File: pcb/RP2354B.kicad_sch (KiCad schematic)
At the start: 29 parts, among them J1 Conn_01x03_MountingPin, SW1 SW_Push, SW2 SW_Push, U2 RP2354B, Y1 ABM8-272-T3

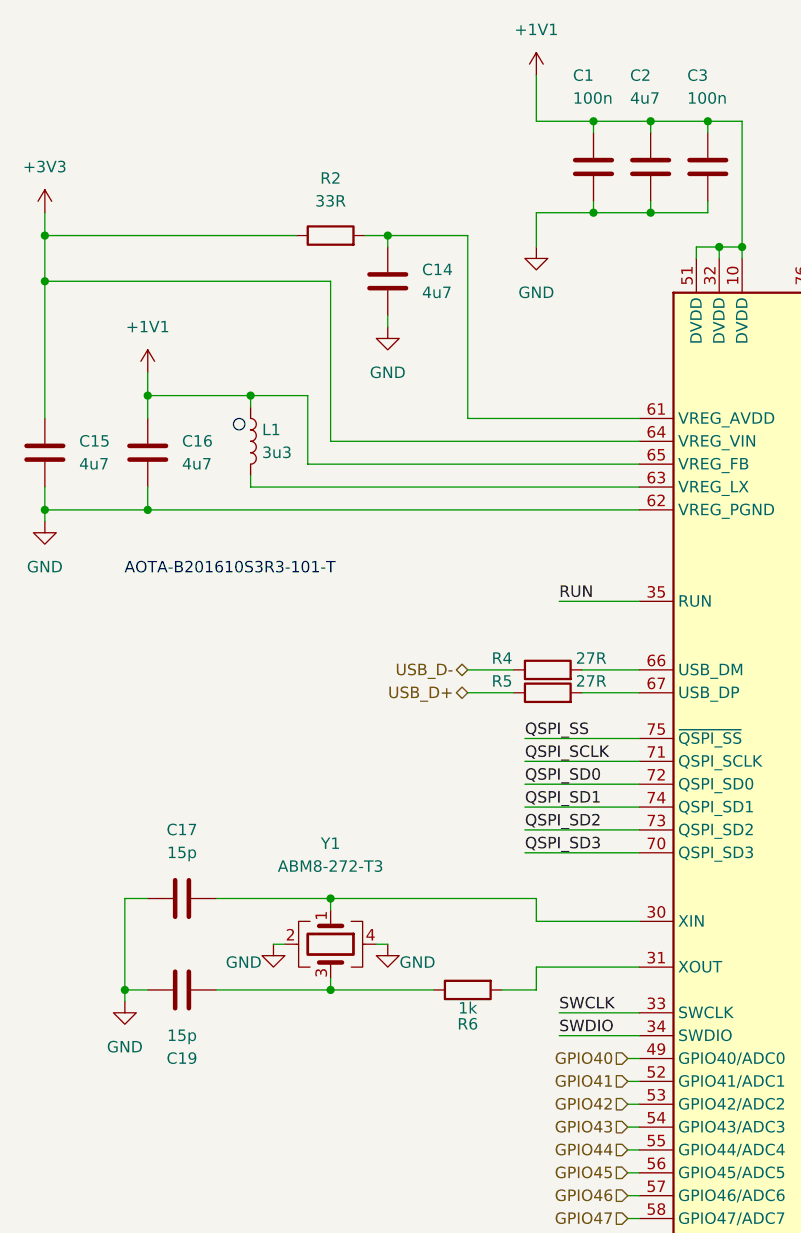
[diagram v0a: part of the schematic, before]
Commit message: Fixed 1V1 trace and added a bit to ADC schematic
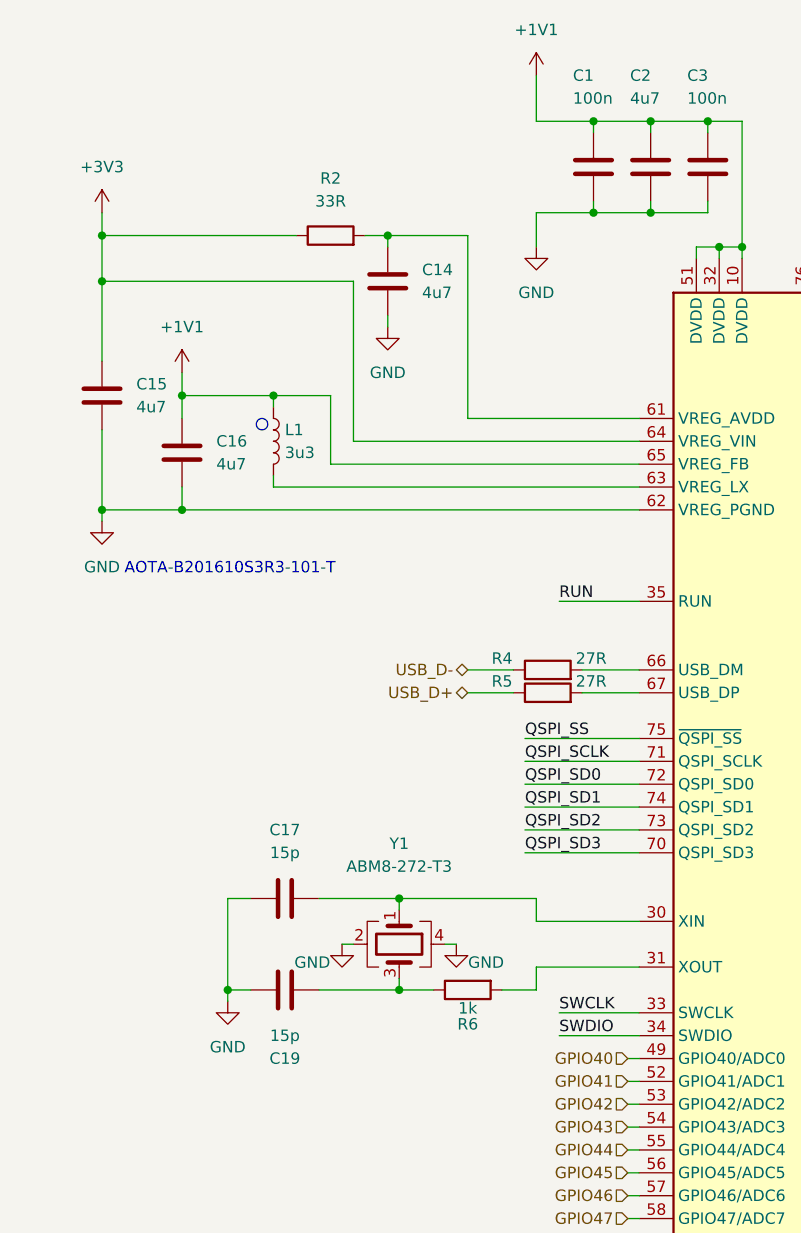
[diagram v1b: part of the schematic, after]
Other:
- moved on the sheet: C15, C16, C17, C19, L1, Y1

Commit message: moved stuff around, started on display
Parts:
- C15, C16: footprint RP2350_80QFN_minimal:C_0402_1005Metric_small_pads -> RP2354B_MINIMAL:C_0402_1005Metric_small_pads
- L1: footprint RP2350_80QFN_minimal:L_pol_2016 -> RP2354B_MINIMAL:L_pol_2016
- U2: footprint RP2350_80QFN_minimal:RP2350-QFN-80-1EP_10x10_P0.4mm_EP3.4x3.4mm_ThermalVias -> RP2354B_MINIMAL:RP2350-QFN-80-1EP_10x10_P0.4mm_EP3.4x3.4mm_ThermalVias
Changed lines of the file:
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@@
 			)
 		)
-		(property "Footprint" "RP2350_80QFN_minimal:C_0402_1005Metric_small_pads"
+		(property "Footprint" "RP2354B_MINIMAL:C_0402_1005Metric_small_pads"
 			(at 32.7152 63.5 0)
 			(hide yes)
@@
 			)
 		)
-		(property "Footprint" "RP2350_80QFN_minimal:L_pol_2016"
+		(property "Footprint" "RP2354B_MINIMAL:L_pol_2016"
 			(at 50.8 64.77 0)
 			(hide yes)
@@
 			)
 		)
-		(property "Footprint" "RP2350_80QFN_minimal:C_0402_1005Metric_small_pads"
+		(property "Footprint" "RP2354B_MINIMAL:C_0402_1005Metric_small_pads"
 			(at 41.6052 69.85 0)
 			(hide yes)
@@
 			)
 		)
-		(property "Footprint" "RP2350_80QFN_minimal:RP2350-QFN-80-1EP_10x10_P0.4mm_EP3.4x3.4mm_ThermalVias"
+		(property "Footprint" "RP2354B_MINIMAL:RP2350-QFN-80-1EP_10x10_P0.4mm_EP3.4x3.4mm_ThermalVias"
 			(at 120.65 101.6 0)
 			(hide yes)

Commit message: worked on power
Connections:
- net USB_D+ renamed D+
- net USB_D- renamed D-

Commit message: worked on io banks
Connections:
- net GPIO0 renamed mod0.GPIO5
- net GPIO1 renamed mod0.GPIO6
- net GPIO10 renamed mod1.GPIO2
- net GPIO11 renamed mod1.GPIO4
- net GPIO12 renamed mod1.GPIO3
- net GPIO13 renamed mod1.GPIO0
- net GPIO14 renamed mod1.GPIO7
- net GPIO15 renamed mod1.GPIO8
- net GPIO16 renamed mod1.GPIO1
- net GPIO17 renamed mod1.GPIO9
- net GPIO18: no longer names the net of U2.18 (GPIO18)
- net GPIO19: no longer names the net of U2.19 (GPIO19)
- net GPIO2 renamed mod0.GPIO2
- net GPIO20 renamed mod1.GPIO5
- net GPIO21 renamed mod1.GPIO6
- net GPIO22: no longer names the net of U2.22 (GPIO22)
- net GPIO23: no longer names the net of U2.23 (GPIO23)
- net GPIO24: no longer names the net of U2.25 (GPIO24)
- net GPIO25: no longer names the net of U2.26 (GPIO25)
- net GPIO26: no longer names the net of U2.27 (GPIO26)
- net GPIO27: no longer names the net of U2.28 (GPIO27)
- net GPIO28: no longer names the net of U2.36 (GPIO28)
- net GPIO29: no longer names the net of U2.37 (GPIO29)
- net GPIO3 renamed mod0.GPIO4
- net GPIO30: no longer names the net of U2.38 (GPIO30)
- net GPIO31: no longer names the net of U2.39 (GPIO31)
- net GPIO32: no longer names the net of U2.40 (GPIO32)
- net GPIO33: no longer names the net of U2.42 (GPIO33)
- net GPIO34: no longer names the net of U2.43 (GPIO34)
- net GPIO35: no longer names the net of U2.44 (GPIO35)
- net GPIO36: no longer names the net of U2.45 (GPIO36)
- net GPIO37: no longer names the net of U2.46 (GPIO37)
- net GPIO38: no longer names the net of U2.47 (GPIO38)
- net GPIO39: no longer names the net of U2.48 (GPIO39)
- net GPIO4 renamed mod0.GPIO3
- net GPIO40: no longer names the net of U2.49 (GPIO40/ADC0)
- net GPIO41: no longer names the net of U2.52 (GPIO41/ADC1)
- net GPIO42: no longer names the net of U2.53 (GPIO42/ADC2)
- net GPIO43: no longer names the net of U2.54 (GPIO43/ADC3)
- net GPIO44: no longer names the net of U2.55 (GPIO44/ADC4)
- net GPIO45: no longer names the net of U2.56 (GPIO45/ADC5)
- net GPIO46: no longer names the net of U2.57 (GPIO46/ADC6)
- net GPIO47: no longer names the net of U2.58 (GPIO47/ADC7)
- net GPIO5 renamed mod0.GPIO7
- net GPIO6 renamed mod0.GPIO1
- net GPIO7 renamed mod0.GPIO0
- net GPIO8 renamed mod0.GPIO9
- net GPIO9 renamed mod0.GPIO8
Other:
- note added: "i2c0, spi1, uart1"
- note added: "i2c1, spi0, uart0"
- moved on the sheet: J1, R1, R3, SW1, SW2

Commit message: did a bunch of gpio bank stuff
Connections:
- net mod0.GPIO7: now also U2.49 (GPIO40/ADC0); no longer U2.2 (GPIO5)
- net mod0.GPIO8: now also U2.52 (GPIO41/ADC1); no longer U2.7 (GPIO9)
- net mod0.GPIO9: now also U2.42 (GPIO33); no longer U2.6 (GPIO8)
- net mod1.GPIO7: now also U2.53 (GPIO42/ADC2); no longer U2.13 (GPIO14)
- net mod1.GPIO8: now also U2.54 (GPIO43/ADC3); no longer U2.14 (GPIO15)
- net mod2.GPIO0: now also U2.19 (GPIO19)
- net mod2.GPIO1: now also U2.18 (GPIO18)
- net mod2.GPIO2: now also U2.22 (GPIO22)
- net mod2.GPIO3: now also U2.40 (GPIO32)
- net mod2.GPIO4: now also U2.23 (GPIO23)
- net mod2.GPIO5: now also U2.36 (GPIO28)
- net mod2.GPIO6: now also U2.37 (GPIO29)
- net mod2.GPIO7: now also U2.55 (GPIO44/ADC4)
- net mod2.GPIO8: now also U2.56 (GPIO45/ADC5)
- net mod2.GPIO9: now also U2.27 (GPIO26)
- net mod3.GPIO0: now also U2.46 (GPIO37)
- net mod3.GPIO1: now also U2.45 (GPIO36)
- net mod3.GPIO2: now also U2.38 (GPIO30)
- net mod3.GPIO3: now also U2.25 (GPIO24)
- net mod3.GPIO4: now also U2.28 (GPIO27)
- net mod3.GPIO5: now also U2.7 (GPIO9)
- net mod3.GPIO6: now also U2.6 (GPIO8)
- net mod3.GPIO7: now also U2.57 (GPIO46/ADC6)
- net mod3.GPIO8: now also U2.58 (GPIO47/ADC7)
- net mod3.GPIO9: now also U2.48 (GPIO39)
- net DISP_DC: now reaches U2.26 (GPIO25)
- net DISP_BACKLIGHT: now reaches U2.39 (GPIO31)
- net spi.SCLK: now reaches U2.43 (GPIO34)
- net spi.MOSI: now reaches U2.44 (GPIO35)
- net DISP_CS: now reaches U2.47 (GPIO38)
- new net ADC_ALERT: U2.2 (GPIO5)
- new net adc.SCL: U2.13 (GPIO14)
- new net adc.SDA: U2.14 (GPIO15)

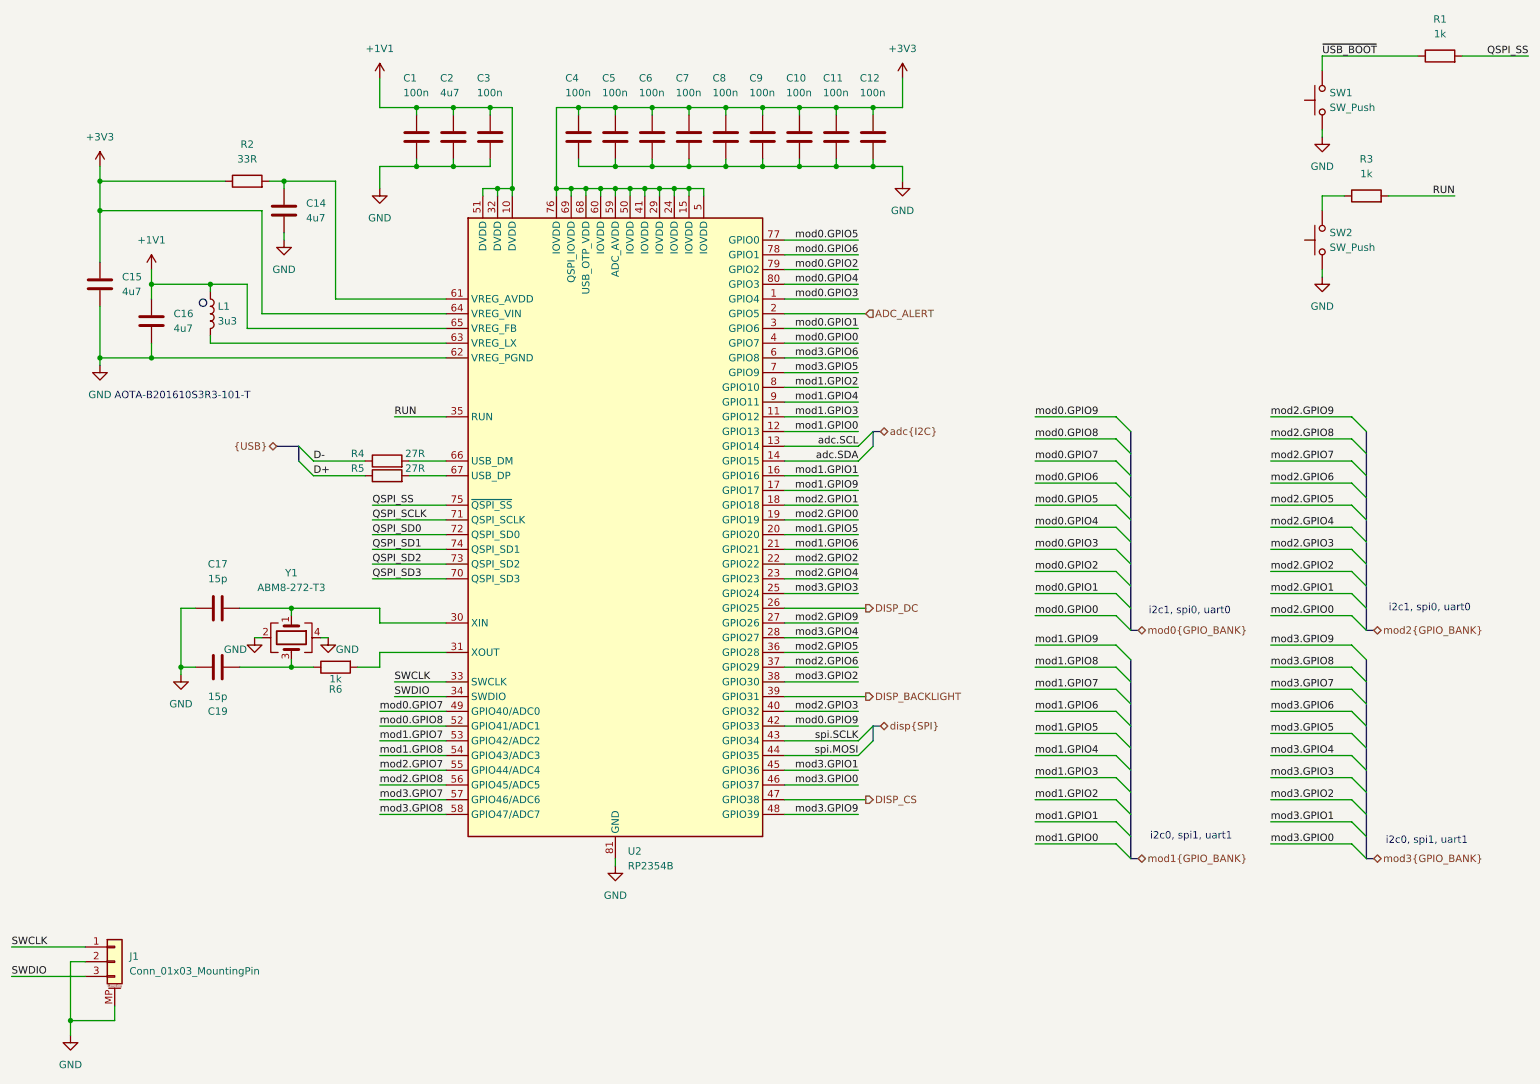
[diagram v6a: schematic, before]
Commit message: started to split up the schematic into two pcbs
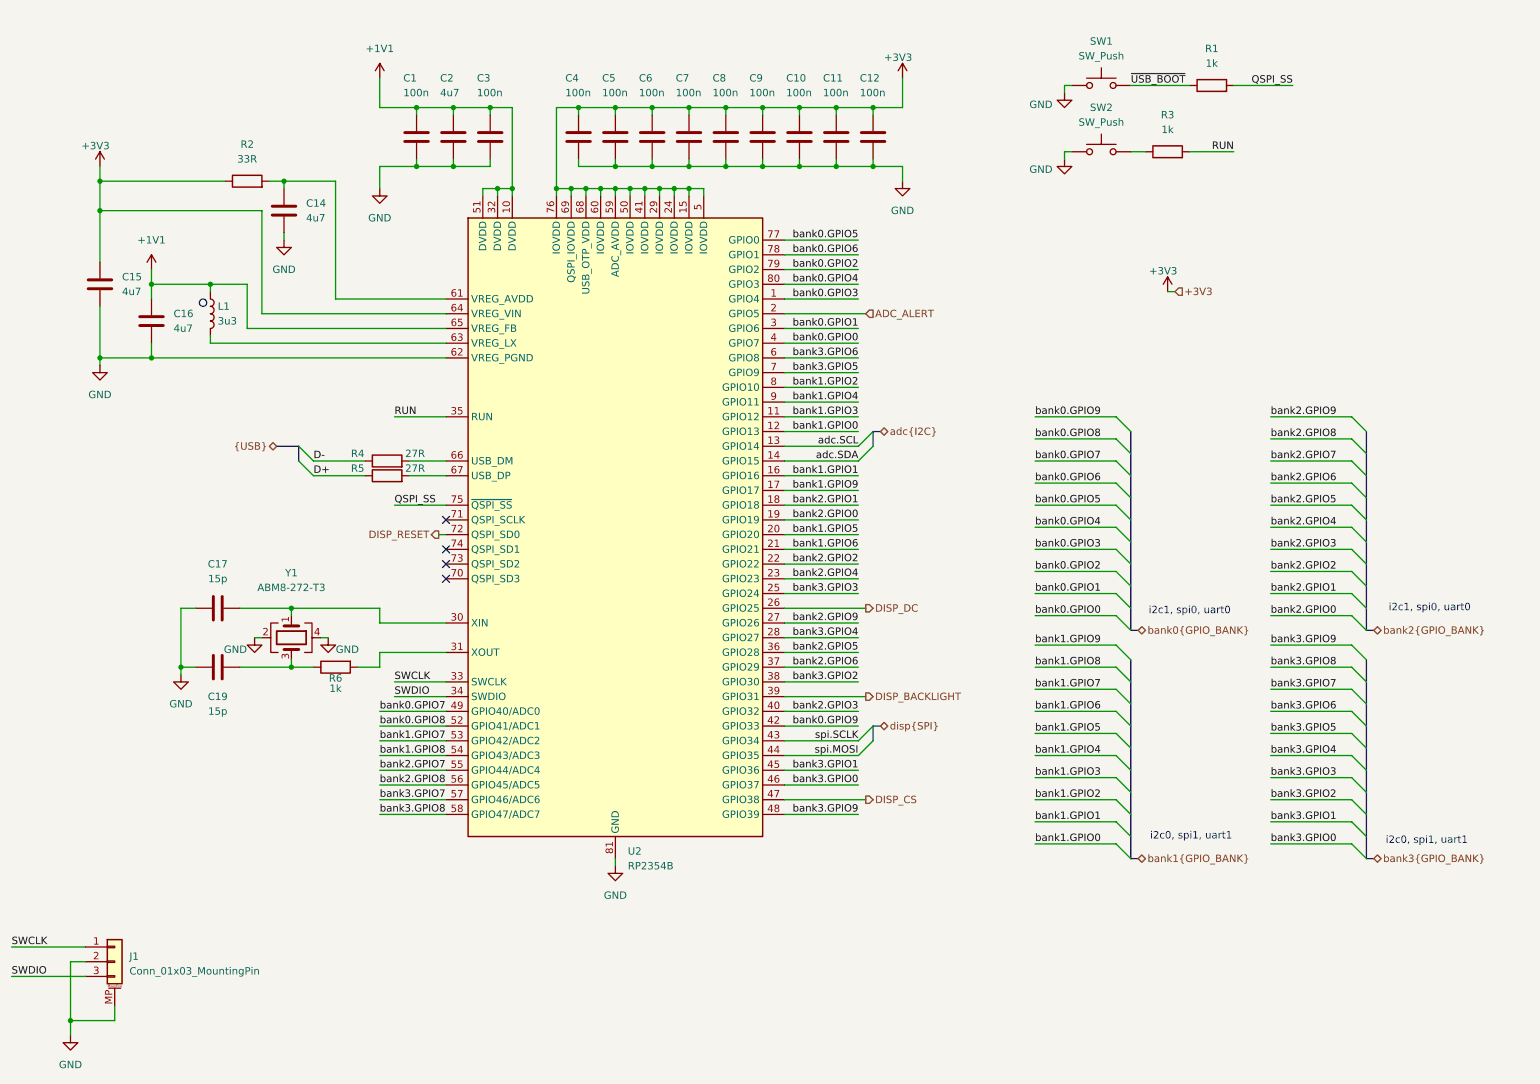
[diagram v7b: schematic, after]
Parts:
- C15, C16: footprint RP2354B_MINIMAL:C_0402_1005Metric_small_pads -> Capacitor_SMD:C_0402_1005Metric
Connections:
- net QSPI_SCLK: no longer names the net of U2.71 (QSPI_SCLK)
- net QSPI_SD0 renamed DISP_RESET
- net QSPI_SD1: no longer names the net of U2.74 (QSPI_SD1)
- net QSPI_SD2: no longer names the net of U2.73 (QSPI_SD2)
- net QSPI_SD3: no longer names the net of U2.70 (QSPI_SD3)
- net mod0.GPIO0 renamed bank0.GPIO0
- net mod0.GPIO1 renamed bank0.GPIO1
- net mod0.GPIO2 renamed bank0.GPIO2
- net mod0.GPIO3 renamed bank0.GPIO3
- net mod0.GPIO4 renamed bank0.GPIO4
- net mod0.GPIO5 renamed bank0.GPIO5
- net mod0.GPIO6 renamed bank0.GPIO6
- net mod0.GPIO7 renamed bank0.GPIO7
- net mod0.GPIO8 renamed bank0.GPIO8
- net mod0.GPIO9 renamed bank0.GPIO9
- net mod1.GPIO0 renamed bank1.GPIO0
- net mod1.GPIO1 renamed bank1.GPIO1
- net mod1.GPIO2 renamed bank1.GPIO2
- net mod1.GPIO3 renamed bank1.GPIO3
- net mod1.GPIO4 renamed bank1.GPIO4
- net mod1.GPIO5 renamed bank1.GPIO5
- net mod1.GPIO6 renamed bank1.GPIO6
- net mod1.GPIO7 renamed bank1.GPIO7
- net mod1.GPIO8 renamed bank1.GPIO8
- net mod1.GPIO9 renamed bank1.GPIO9
- net mod2.GPIO0 renamed bank2.GPIO0
- net mod2.GPIO1 renamed bank2.GPIO1
- net mod2.GPIO2 renamed bank2.GPIO2
- net mod2.GPIO3 renamed bank2.GPIO3
- net mod2.GPIO4 renamed bank2.GPIO4
- net mod2.GPIO5 renamed bank2.GPIO5
- net mod2.GPIO6 renamed bank2.GPIO6
- net mod2.GPIO7 renamed bank2.GPIO7
- net mod2.GPIO8 renamed bank2.GPIO8
- net mod2.GPIO9 renamed bank2.GPIO9
- net mod3.GPIO0 renamed bank3.GPIO0
- net mod3.GPIO1 renamed bank3.GPIO1
- net mod3.GPIO2 renamed bank3.GPIO2
- net mod3.GPIO3 renamed bank3.GPIO3
- net mod3.GPIO4 renamed bank3.GPIO4
- net mod3.GPIO5 renamed bank3.GPIO5
- net mod3.GPIO6 renamed bank3.GPIO6
- net mod3.GPIO7 renamed bank3.GPIO7
- net mod3.GPIO8 renamed bank3.GPIO8
- net mod3.GPIO9 renamed bank3.GPIO9
- no-connect marks 0 -> 4
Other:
- note removed: "AOTA-B201610S3R3-101-T"
- moved on the sheet: R1, R3, SW1, SW2
